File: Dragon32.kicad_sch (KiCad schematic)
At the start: 5 parts, among them IC25 LM393P, IC31 74LS02N

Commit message: add uart to board
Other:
- added sheet Serial (serial.kicad_sch)
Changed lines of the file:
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@@
+	)
+	(sheet
+		(at 299.72 210.82)
+		(size 27.94 17.78)
+		(exclude_from_sim no)
+		(in_bom yes)
+		(on_board yes)
+		(dnp no)
+		(fields_autoplaced yes)
+		(stroke
+			(width 0.1524)
+			(type solid)
+		)
+		(fill
+			(color 0 0 0 0.0000)
+		)
+		(property "Sheetname" "Serial"
+			(at 299.72 210.1084 0)
+			(effects
+				(font
+					(size 1.27 1.27)
+				)
+				(justify left bottom)
+			)
+		)
+		(property "Sheetfile" "serial.kicad_sch"
+			(at 299.72 229.1846 0)
+			(effects
+				(font
+					(size 1.27 1.27)
+				)
+				(justify left top)
+			)
+		)
+		(instances
+			(project "Dragon32"
+				(path "/0c3dceba-7c95-4b3d-b590-0eb581444beb"
+					(page "9")
+				)
+			)
+		)
 	)
 	(sheet

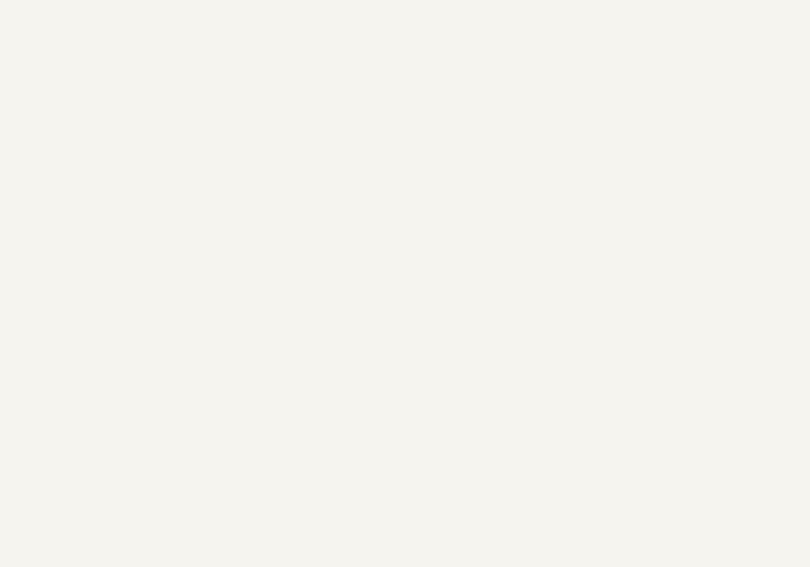
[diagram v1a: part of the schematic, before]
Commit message: update to keyboard switch option
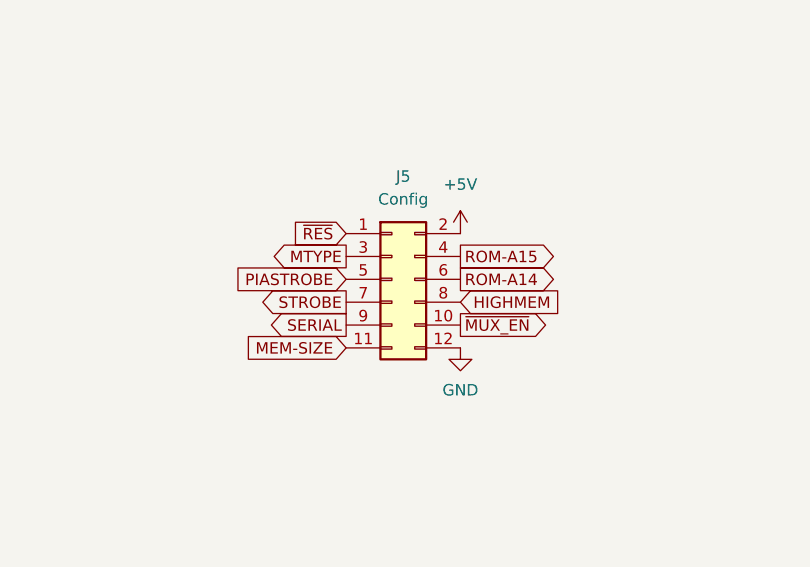
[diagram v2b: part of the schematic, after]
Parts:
- added J5: Config, Connector_PinHeader_2.54mm:PinHeader_2x06_P2.54mm_Vertical, symbol Connector_Generic:Conn_02x06_Odd_Even
- IC25: LCSC (none) -> C5209
- IC31: LCSC (none) -> C22374091; SA2120 Sheet 1 (spare) -> (none)
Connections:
- net +5V: now also J5.2 (Pin_2)
- net GND: now also J5.12 (Pin_12)
- net ~{RES}: now also J5.1 (Pin_1)
- new net HIGHMEM: J5.8 (Pin_8)
- new net MEM-SIZE: J5.11 (Pin_11)
- new net MTYPE: J5.3 (Pin_3)
- new net PIASTROBE: J5.5 (Pin_5)
- new net ROM-A14: J5.6 (Pin_6)
- new net ROM-A15: J5.4 (Pin_4)
- new net SERIAL: J5.9 (Pin_9)
- new net STROBE: J5.7 (Pin_7)
- new net ~{MUX_EN}: J5.10 (Pin_10)
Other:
- company: Dragon Data -> (none)
- title: Dragon 32 CPU UK PAL -> Dragon CPU UK Revised
